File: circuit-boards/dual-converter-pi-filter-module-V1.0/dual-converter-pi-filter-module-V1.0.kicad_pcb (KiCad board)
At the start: 4 copper layers, 83 x 70 mm, 57 parts

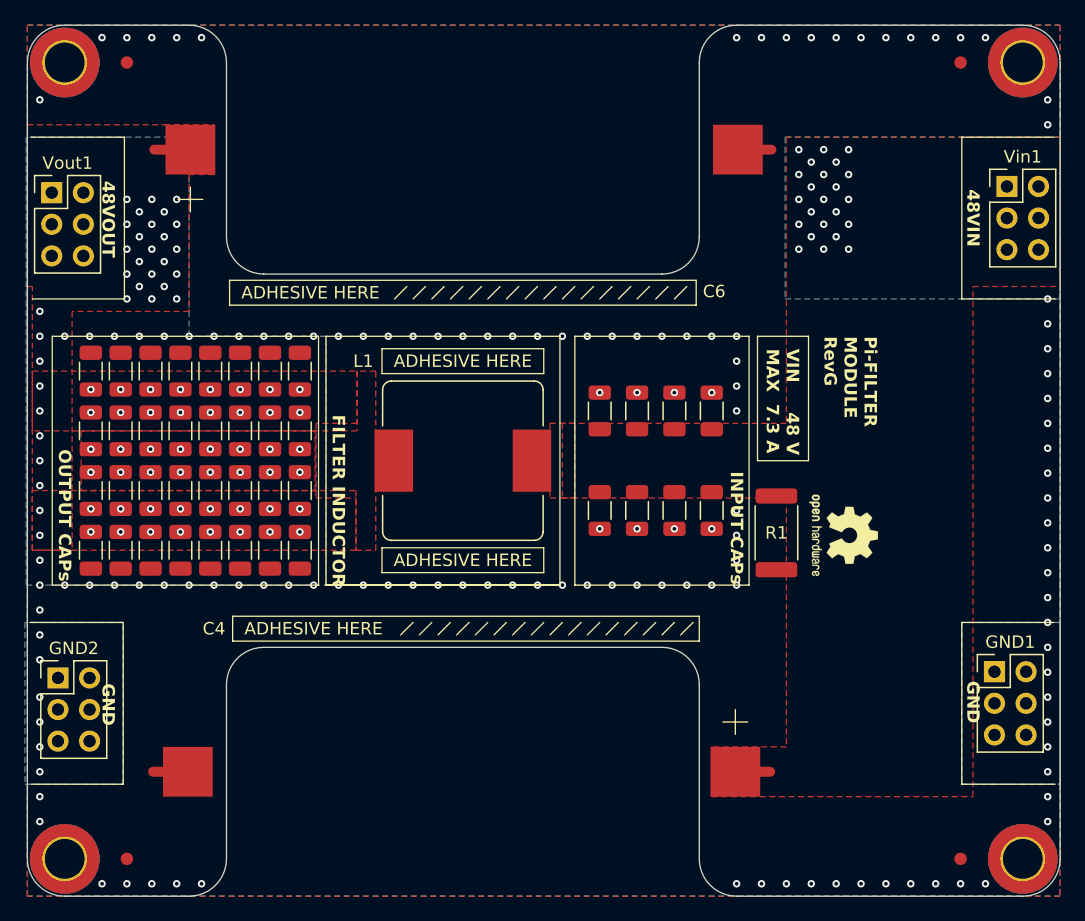
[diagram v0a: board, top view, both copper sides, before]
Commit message: pifilter: align and lock connectors and mountpoints
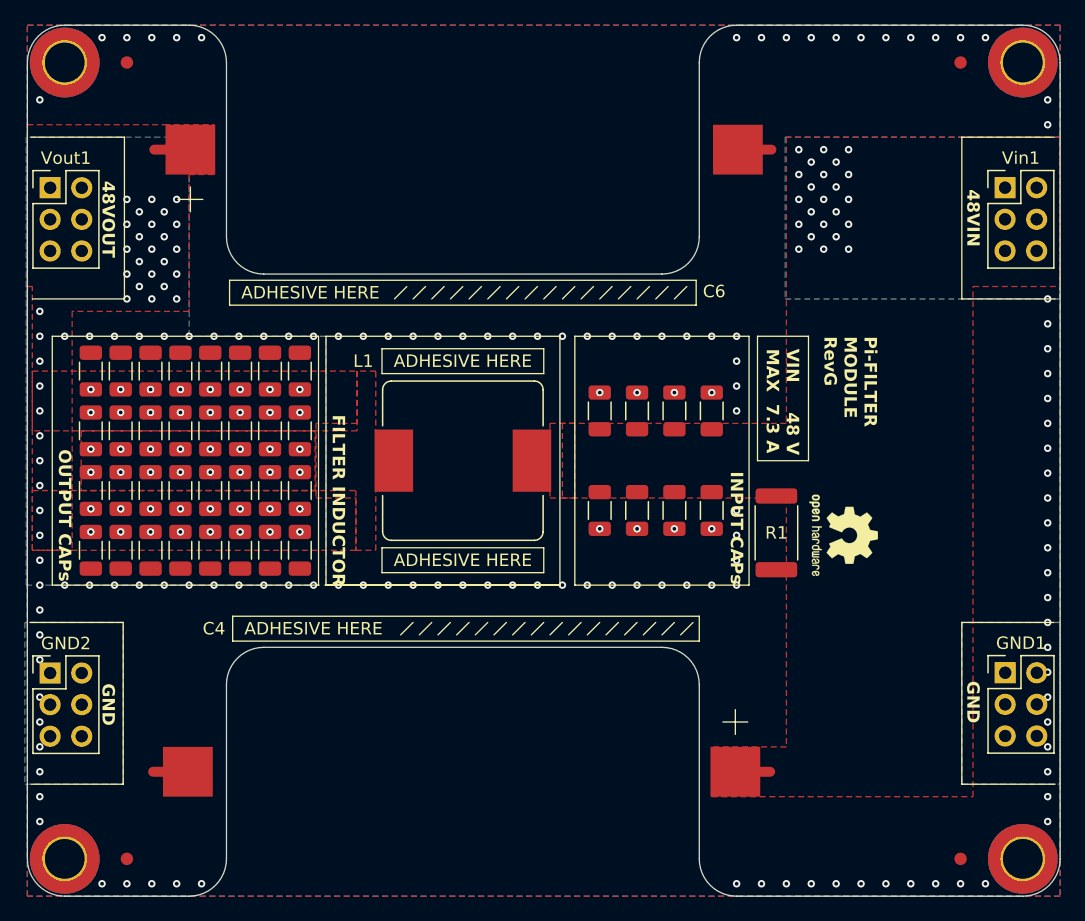
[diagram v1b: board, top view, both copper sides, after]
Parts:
- moved GND1 0.86 mm to (115.6, 69.0)
- moved GND2 0.74 mm to (38.8, 69.1)
- moved Vout1 0.42 mm to (38.8, 30.1)
- moved Vin1 0.18 mm to (115.6, 30.1)
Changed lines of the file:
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@@
 	)
 	(footprint "Connector_PinHeader_2.54mm:PinHeader_2x03_P2.54mm_Vertical"
+		(locked yes)
 		(layer "F.Cu")
-		(at 115.725 29.96)
+		(at 115.575 30.06)
 		(descr "Through hole straight pin header, 2x03, 2.54mm pitch, double rows")
 		(tags "Through hole pin header THT 2x03 2.54mm double row")
@@
 	)
 	(footprint "Connector_PinHeader_2.54mm:PinHeader_2x03_P2.54mm_Vertical"
+		(locked yes)
 		(layer "F.Cu")
-		(at 114.725 68.96)
+		(at 115.585221 69.04314)
 		(descr "Through hole straight pin header, 2x03, 2.54mm pitch, double rows")
 		(tags "Through hole pin header THT 2x03 2.54mm double row")
@@
 	)
 	(footprint "Connector_PinHeader_2.54mm:PinHeader_2x03_P2.54mm_Vertical"
+		(locked yes)
 		(layer "F.Cu")
-		(at 39.46 69.46)
+		(at 38.828597 69.066989)
 		(descr "Through hole straight pin header, 2x03, 2.54mm pitch, double rows")
 		(tags "Through hole pin header THT 2x03 2.54mm double row")
@@
 	)
 	(footprint "Connector_PinHeader_2.54mm:PinHeader_2x03_P2.54mm_Vertical"
+		(locked yes)
 		(layer "F.Cu")
-		(at 38.96 30.46)
+		(at 38.830892 30.065064)
 		(descr "Through hole straight pin header, 2x03, 2.54mm pitch, double rows")
 		(tags "Through hole pin header THT 2x03 2.54mm double row")
@@
 		(hatch edge 0.5)
 		(priority 1)
-		(connect_pads
+		(connect_pads yes
 			(clearance 0.25)
 		)

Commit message: final drc checks, silkscreen edits, added stitching vias to motherboard and pi filter
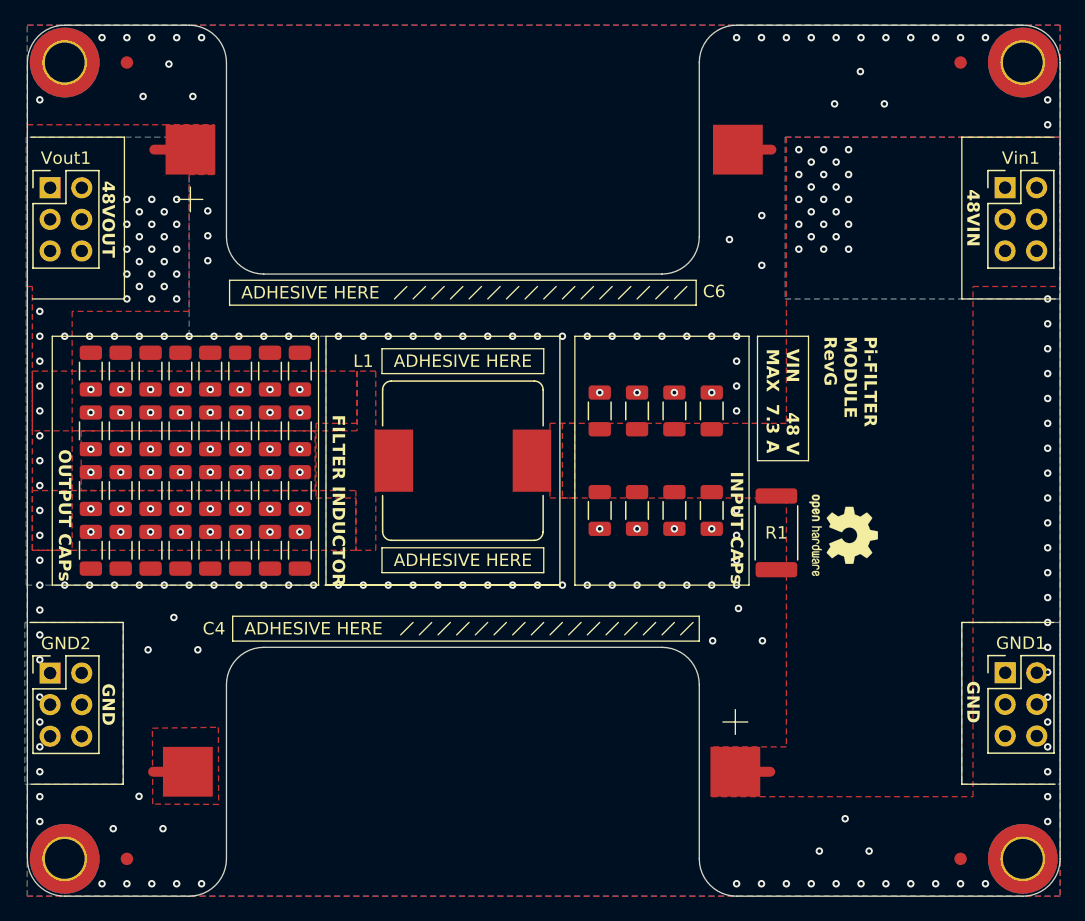
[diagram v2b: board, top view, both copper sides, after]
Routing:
- net GND: vias 164 -> 188
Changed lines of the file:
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@@
+	)
+	(via
+		(at 104.65 83.375)
+		(size 0.6)
+		(drill 0.3)
+		(layers "F.Cu" "B.Cu")
+		(free yes)
+		(net 1)
 	)
 	(via
@@
 	)
 	(via
+		(at 103.95 20.725)
+		(size 0.6)
+		(drill 0.3)
+		(layers "F.Cu" "B.Cu")
+		(free yes)
+		(net 1)
+	)
+	(via
 		(at 43 18)
 		(size 0.6)
@@
 	)
 	(via
+		(at 93.425 34.225)
+		(size 0.6)
+		(drill 0.3)
+		(layers "F.Cu" "B.Cu")
+		(free yes)
+		(net 1)
+	)
+	(via
 		(at 98 86)
 		(size 0.6)
@@
 	)
 	(via
+		(at 48.775 64.6)
+		(size 0.6)
+		(drill 0.3)
+		(layers "F.Cu" "B.Cu")
+		(free yes)
+		(net 1)
+	)
+	(via
 		(at 38 60)
 		(size 0.6)
@@
 	)
 	(via
+		(at 96.025 32.3)
+		(size 0.6)
+		(drill 0.3)
+		(layers "F.Cu" "B.Cu")
+		(free yes)
+		(net 1)
+	)
+	(via
 		(at 94 56)
 		(size 0.6)
@@
 	)
 	(via
+		(at 46.7 67.2)
+		(size 0.6)
+		(drill 0.3)
+		(layers "F.Cu" "B.Cu")
+		(free yes)
+		(net 1)
+	)
+	(via
 		(at 46 42)
 		(size 0.6)
@@
 	)
 	(via
+		(at 50.3 22.725)
+		(size 0.6)
+		(drill 0.3)
+		(layers "F.Cu" "B.Cu")
+		(free yes)
+		(net 1)
+	)
+	(via
 		(at 94 18)
 		(size 0.6)
@@
 	)
 	(via
+		(at 102.725 80.775)
+		(size 0.6)
+		(drill 0.3)
+		(layers "F.Cu" "B.Cu")
+		(free yes)
+		(net 1)
+	)
+	(via
+		(at 105.875 23.325)
+		(size 0.6)
+		(drill 0.3)
+		(layers "F.Cu" "B.Cu")
+		(free yes)
+		(net 1)
+	)
+	(via
 		(at 56.5 52.925)
 		(size 0.6)
@@
 	)
 	(via
+		(at 51.5 31.925)
+		(size 0.6)
+		(drill 0.3)
+		(layers "F.Cu" "B.Cu")
+		(free yes)
+		(net 1)
+	)
+	(via
 		(at 96 86)
 		(size 0.6)
@@
 	)
 	(via
+		(at 51.5 33.925)
+		(size 0.6)
+		(drill 0.3)
+		(layers "F.Cu" "B.Cu")
+		(free yes)
+		(net 1)
+	)
+	(via
+		(at 96.025 36.3)
+		(size 0.6)
+		(drill 0.3)
+		(layers "F.Cu" "B.Cu")
+		(free yes)
+		(net 1)
+	)
+	(via
 		(at 72 62)
 		(size 0.6)
@@
 	)
 	(via
+		(at 51.5 35.925)
+		(size 0.6)
+		(drill 0.3)
+		(layers "F.Cu" "B.Cu")
+		(free yes)
+		(net 1)
+	)
+	(via
 		(at 94 42)
 		(size 0.6)
@@
 	)
 	(via
+		(at 46.3 22.725)
+		(size 0.6)
+		(drill 0.3)
+		(layers "F.Cu" "B.Cu")
+		(free yes)
+		(net 1)
+	)
+	(via
 		(at 92 42)
 		(size 0.6)
@@
 	)
 	(via
+		(at 48.375 20.125)
+		(size 0.6)
+		(drill 0.3)
+		(layers "F.Cu" "B.Cu")
+		(free yes)
+		(net 1)
+	)
+	(via
 		(at 38 46)
 		(size 0.6)
@@
 	)
 	(via
+		(at 50.7 67.2)
+		(size 0.6)
+		(drill 0.3)
+		(layers "F.Cu" "B.Cu")
+		(free yes)
+		(net 1)
+	)
+	(via
 		(at 54.1 51.075)
 		(size 0.6)
@@
 	)
 	(via
+		(at 101.875 23.325)
+		(size 0.6)
+		(drill 0.3)
+		(layers "F.Cu" "B.Cu")
+		(free yes)
+		(net 1)
+	)
+	(via
 		(at 88 42)
 		(size 0.6)
@@
 	)
 	(via
+		(at 92.075 66.475)
+		(size 0.6)
+		(drill 0.3)
+		(layers "F.Cu" "B.Cu")
+		(free yes)
+		(net 1)
+	)
+	(via
 		(at 42.1 52.925)
 		(size 0.6)
@@
 	)
 	(via
+		(at 43.9 81.575)
+		(size 0.6)
+		(drill 0.3)
+		(layers "F.Cu" "B.Cu")
+		(free yes)
+		(net 1)
+	)
+	(via
 		(at 119 59)
 		(size 0.6)
@@
 	)
 	(via
+		(at 100.65 83.375)
+		(size 0.6)
+		(drill 0.3)
+		(layers "F.Cu" "B.Cu")
+		(free yes)
+		(net 1)
+	)
+	(via
 		(at 84 62)
 		(size 0.6)
@@
 	)
 	(via
+		(at 94.15 63.875)
+		(size 0.6)
+		(drill 0.3)
+		(layers "F.Cu" "B.Cu")
+		(free yes)
+		(net 1)
+	)
+	(via
 		(at 119 45)
 		(size 0.6)
@@
 	)
 	(via
+		(at 47.9 81.575)
+		(size 0.6)
+		(drill 0.3)
+		(layers "F.Cu" "B.Cu")
+		(free yes)
+		(net 1)
+	)
+	(via
+		(at 45.975 78.975)
+		(size 0.6)
+		(drill 0.3)
+		(layers "F.Cu" "B.Cu")
+		(free yes)
+		(net 1)
+	)
+	(via
 		(at 119 79)
 		(size 0.6)
@@
 	(via
 		(at 119 47)
+		(size 0.6)
+		(drill 0.3)
+		(layers "F.Cu" "B.Cu")
+		(free yes)
+		(net 1)
+	)
+	(via
+		(at 96.075 66.475)
 		(size 0.6)
 		(drill 0.3)
@@
 			)
 		)
+	)
+	(zone
+		(net 1)
+		(net_name "GND")
+		(layer "F.Cu")
+		(hatch edge 0.5)
+		(priority 4)
+		(connect_pads
+			(clearance 0.25)
+		)
+		(min_thickness 0.25)
+		(filled_areas_thickness no)
+		(fill yes
+			(thermal_gap 0.25)
+			(thermal_bridge_width 0.8)
+		)
+		(polygon
+			(pts
+				(xy 47.05 73.5) (xy 52.35 73.425) (xy 52.375 79.625) (xy 47.075 79.6)
+			)
+		)
